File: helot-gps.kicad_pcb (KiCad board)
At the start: 2 copper layers, 50 x 37 mm, 69 parts, among them P1 SMA_1, P2 FCONN_1, P3 FCONN_2, P4 HELOT_PCIE, P5 HEADER, U1 MAX2112, U2 MAX2112

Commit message: routing
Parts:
- added HOLE_M3: Val**, HOLE_M3, F.Cu at (104.0, 104.0)
- added HOLE_M3: Val**, HOLE_M3, F.Cu at (146.0, 104.0)
- moved C22 153.2 mm to (74.0, 144.0)
- moved C21 138.7 mm to (83.0, 140.0)
- moved C19 138.2 mm to (82.0, 137.0)
- moved L4 135.0 mm to (106.5, 131.5)
- moved C11 133.3 mm to (81.0, 134.0)
- moved P2 132.0 mm to (117.0, 107.0)
- moved C13 131.1 mm to (79.0, 146.0)
- moved R1 130.7 mm to (109.5, 122.5), turned to 270 degrees
- moved R8 128.5 mm to (109.0, 127.0)
- moved C16 126.7 mm to (107.0, 121.5), turned to 180 degrees
- moved P1 126.1 mm to (105.0, 113.0)
- moved R6 125.9 mm to (123.0, 163.0)
- moved L3 125.2 mm to (117.0, 114.0), turned to 180 degrees
- moved C23 123.6 mm to (104.5, 124.0), turned to 270 degrees
- moved C33 119.9 mm to (116.0, 130.0), turned to 270 degrees
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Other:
- board size 50 x 37 mm -> 50 x 41 mm

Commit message: some simple stuff done (just saving my progress)
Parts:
- moved C22 51.3 mm to (121.5, 124.5)
- moved C3 47.6 mm to (128.5, 119.0), turned to 180 degrees
- moved C9 46.0 mm to (130.0, 131.0), turned to 270 degrees
- moved C19 43.2 mm to (121.5, 119.5)
- moved C14 41.5 mm to (128.5, 120.5), turned to 180 degrees
- moved C6 37.2 mm to (121.5, 121.0)
- moved R11 34.7 mm to (144.0, 137.5), turned to 270 degrees
- moved C13 33.6 mm to (108.0, 129.0), turned to 180 degrees
- moved C12 33.5 mm to (128.5, 128.0), turned to 180 degrees
- moved R7 32.3 mm to (142.0, 137.5), turned to 270 degrees
- moved C11 32.2 mm to (110.0, 120.0), turned to 180 degrees
- moved C21 31.6 mm to (113.0, 130.0), turned to 270 degrees
- moved L2 30.9 mm to (124.5, 135.0), turned to 180 degrees
- moved C20 30.5 mm to (124.5, 133.0)
- moved C31 29.4 mm to (140.5, 137.5), turned to 270 degrees
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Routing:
- net GND: track 0.00 -> 185.2 mm
- net /VCC2: track 0.00 -> 39.6 mm
- net N-000001: track 0.00 -> 19.4 mm
- net N-000003: track 0.00 -> 19.2 mm
- net N-000004: track 0.00 -> 18.9 mm
- net N-000005: track 0.00 -> 18.7 mm
- net N-0000047: track 0.00 -> 18.3 mm
- net N-0000045: track 0.00 -> 18.1 mm
- net N-0000044: track 0.00 -> 17.9 mm
- net N-0000042: track 0.00 -> 17.7 mm
- net /SDA: track 0.00 -> 11.7 mm
- net /SCL: track 0.00 -> 9.20 mm
- net N-0000028: track 0.00 -> 6.61 mm
- net N-0000027: track 0.00 -> 6.57 mm
- net N-0000023: track 0.00 -> 5.71 mm
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- added copper zone on F.Cu, net /75R_3
- added copper zone on F.Cu, net /75R_4
- added copper zone on B.Cu, net GND
- added copper zone on F.Cu, net GND
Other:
- net class 50Ohm added: clearance 0.15, trace_width 2.95, via_dia 0.6, via_drill 0.3
- net class 75Ohm added: clearance 0.15, trace_width 1.45, via_dia 0.6, via_drill 0.3
- net class Default: clearance 0.254 -> 0.15; trace_width 0.254 -> 0.15; via_dia 0.889 -> 0.6; via_drill 0.635 -> 0.3
- net class Power added: clearance 0.15, trace_width 0.25, via_dia 0.6, via_drill 0.3
- rule trace_clearance: 0.254 -> 0.15
- rule trace_min: 0.254 -> 0.15
- rule via_min_drill: 0.508 -> 0.3
- rule via_min_size: 0.889 -> 0.6

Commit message: one more
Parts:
- moved C31 1.80 mm to (142.0, 136.5)
- moved R7 1.80 mm to (140.5, 136.5)
- moved C30 1.00 mm to (140.5, 133.5)
- moved C44 1.00 mm to (145.5, 133.5)
- moved C45 1.00 mm to (145.5, 136.5)
- moved R10 1.00 mm to (144.0, 133.5)
- moved R11 1.00 mm to (144.0, 136.5)
- moved R5 1.00 mm to (142.0, 133.5)
- moved R6 0.50 mm to (135.5, 136.5)
- moved R9 0.50 mm to (135.5, 138.5)
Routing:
- net /DP2: track 3.98 -> 15.0 mm
- net /DAC1: track 0.00 -> 11.0 mm
- net /DP1: track 4.37 -> 12.8 mm
- net /DAC2: track 0.00 -> 7.66 mm
- net N-000009: track 0.00 -> 2.70 mm
- net N-0000010: track 0.00 -> 2.70 mm
- net /3.3V: track 0.00 -> 2.54 mm
- net /SCL: track 9.20 -> 10.0 mm
- net /SDA: track 11.7 -> 12.5 mm

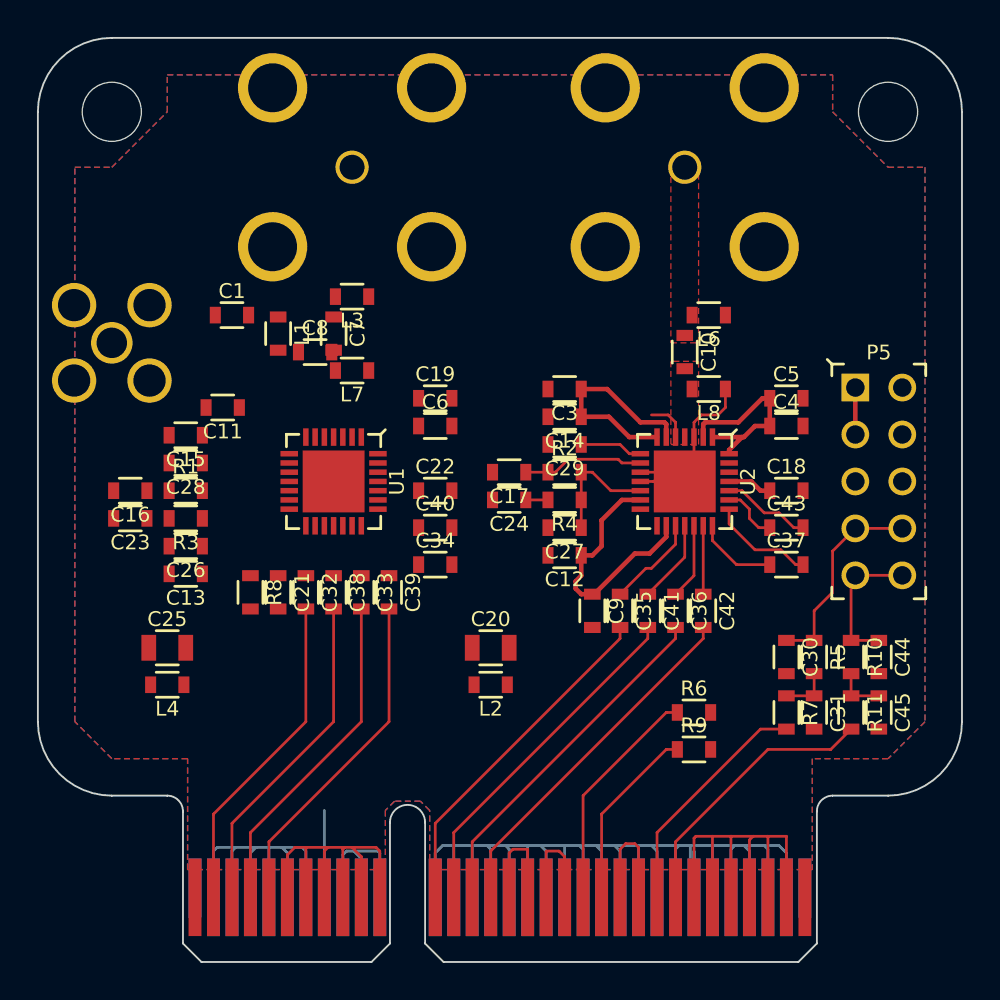
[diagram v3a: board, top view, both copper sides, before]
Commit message: need to clear some area around the rf traces
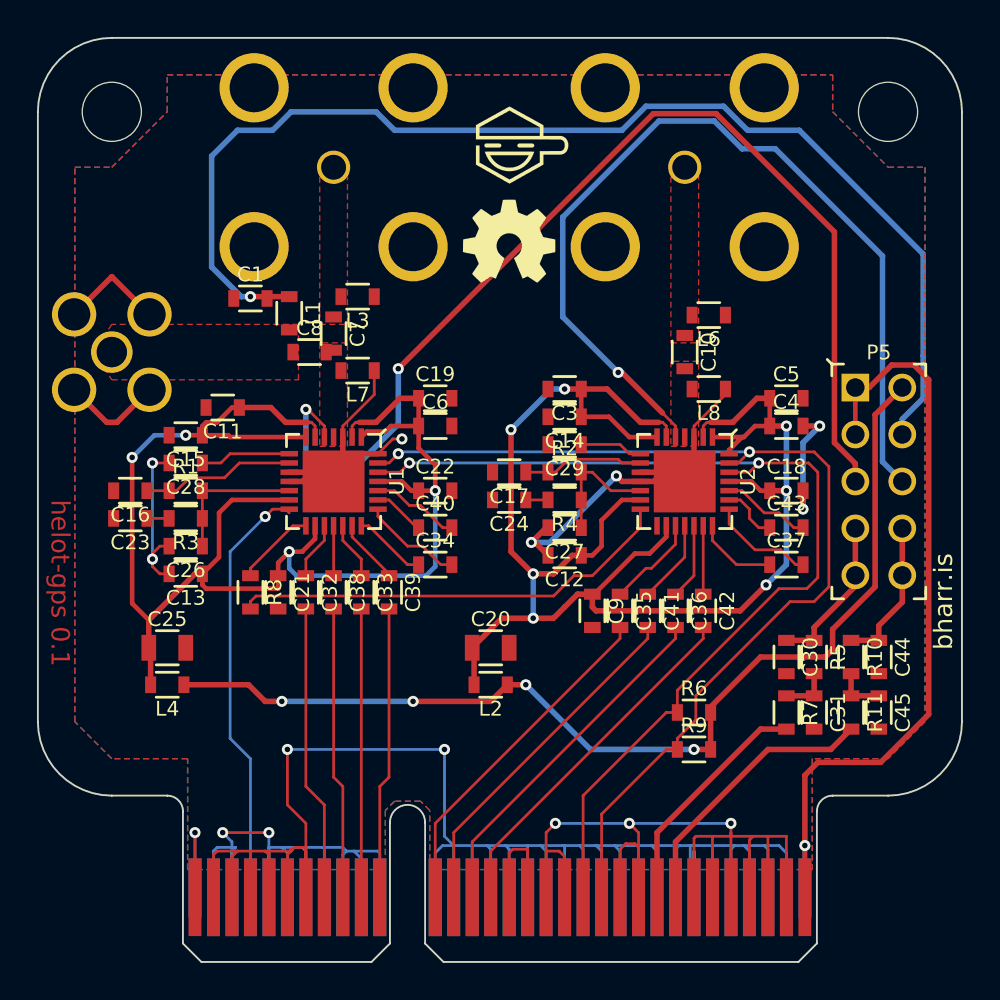
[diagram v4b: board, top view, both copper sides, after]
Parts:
- added G***: OSHW_silkscreen-front_5mm, OSHW_silkscreen-front_5mm, F.Cu at (125.5, 111.0)
- added G***: bharr_silkscreen-front_5mm, bharr_silkscreen-front_5mm, F.Cu at (126.2, 105.8)
- moved C1 1.35 mm to (111.5, 114.1)
- moved L1 1.25 mm to (113.6, 114.9)
- moved P2 1.00 mm to (116.0, 107.0)
- moved P1 0.50 mm to (104.0, 117.0)
- moved C8 0.30 mm to (114.7, 117.0)
- moved L3 0.30 mm to (117.3, 114.0)
- moved L7 0.30 mm to (117.3, 118.0)
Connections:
- C32 pad 2: N-0000042 (its old number) -> N-0000037
- C33 pad 2: N-0000045 (its old number) -> N-0000035
- C38 pad 2: N-0000044 (its old number) -> N-0000036
- C39 pad 2: N-0000047 (its old number) -> N-0000034
- P4 pad 1: /3.3V -> N-0000010
- P4 pad 15: GND -> N-0000037
- P4 pad 16: /CLK -> GND
- P4 pad 17: GND -> N-0000036
- P4 pad 19: GND -> N-0000035
- P4 pad 2: /3.3V -> N-0000010
- P4 pad 21: GND -> N-0000034
- P4 pad 3: N-0000042 (its old number) -> GND
- P4 pad 5: N-0000044 (its old number) -> GND
- P4 pad 63: N-000008 -> /3.3V
- P4 pad 64: N-000008 -> /3.3V
- P4 pad 7: N-0000045 (its old number) -> GND
- P4 pad 8: GND -> /CLK
- P4 pad 9: N-0000047 (its old number) -> GND
- P5 pad 8: /DAC1 -> /DAC2
- P5 pad 9: /DAC2 -> /DAC1
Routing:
- net GND: track 185.2 -> 280.7 mm, vias 0 -> 14
- net /VCC1: track 0.00 -> 81.9 mm, vias 0 -> 4
- net /ANT_PWR: track 0.00 -> 64.9 mm, vias 0 -> 1
- net /GC1: track 0.00 -> 60.3 mm, vias 0 -> 2
- net /VCC: track 0.00 -> 56.6 mm, vias 0 -> 4
- net /GC2: track 2.27 -> 49.7 mm, vias 0 -> 1
- net /VCC2: track 39.6 -> 86.3 mm, vias 0 -> 7
- net /SCL: track 10.0 -> 55.8 mm, vias 0 -> 2
- net /SDA: track 12.5 -> 55.5 mm, vias 0 -> 2
- net /3.3V: track 2.54 -> 42.4 mm, vias 0 -> 1
- net /CLK_2: track 0.00 -> 24.2 mm
- net /CLK: track 4.70 -> 23.4 mm, vias 0 -> 1
- net N-0000047 (its old number): track 18.3 -> 0.00 mm
- net N-0000045 (its old number): track 18.1 -> 0.00 mm
- net N-0000044 (its old number): track 17.9 -> 0.00 mm
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- added copper zone on F.Cu, net /50R_1
- added copper zone on F.Cu, net /75R_1
- added copper zone on F.Cu, net /75R_2
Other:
- board text added: "bharr.is"
- board text added: "helot-gps 0.1"

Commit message: 0.1
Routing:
- net GND: track 280.7 -> 337.1 mm, vias 14 -> 25
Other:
- board text added: "3.3 VCC 3.3 ANT G1 G2 A1 A2 A1 A2"
